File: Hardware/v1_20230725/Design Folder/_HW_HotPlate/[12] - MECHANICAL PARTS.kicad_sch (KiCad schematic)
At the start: 15 parts, among them P1201 MHDR_4X2_RA_2.54MM

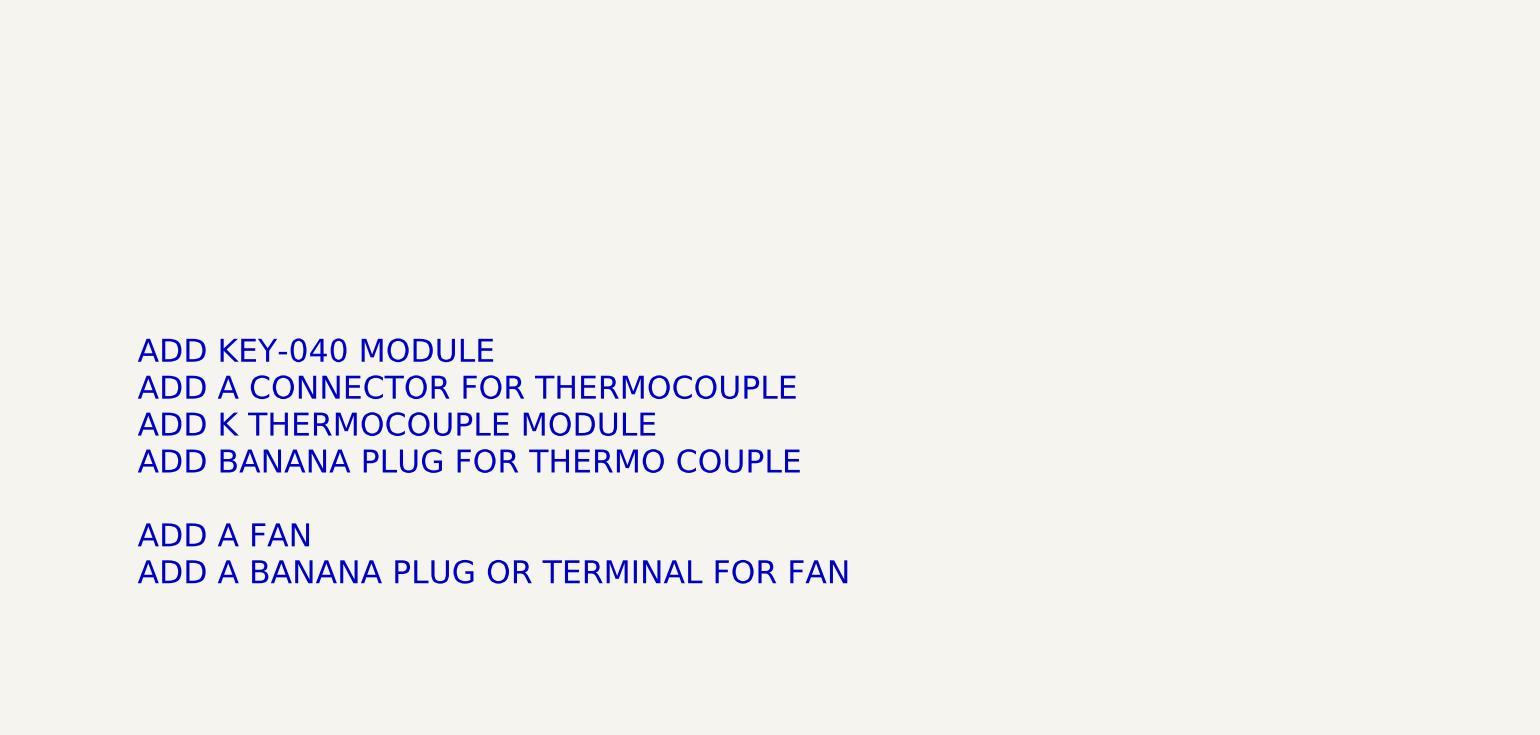
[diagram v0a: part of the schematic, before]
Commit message: Adding some items to todo list
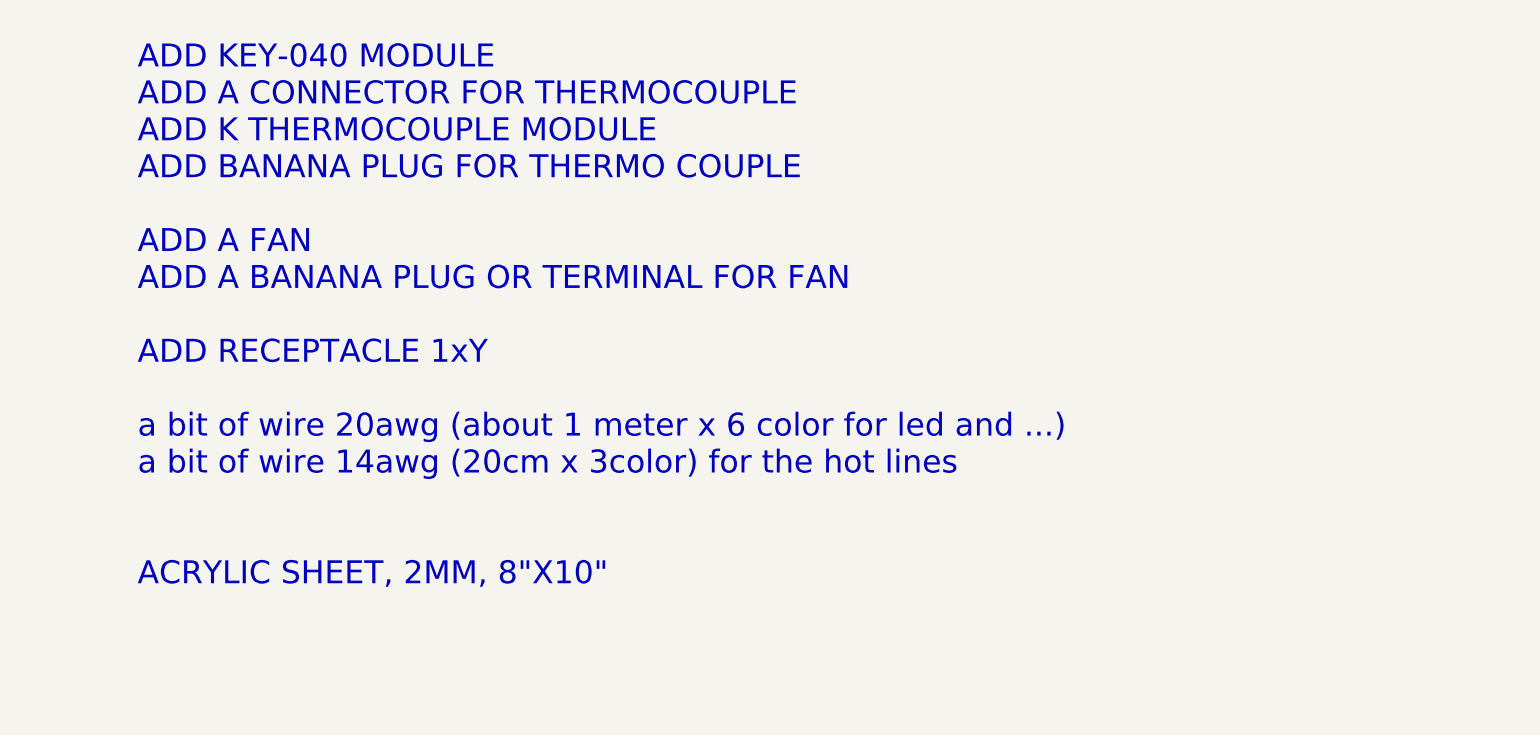
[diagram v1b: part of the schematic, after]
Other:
- note added: "ADD KEY-040 MODULE ADD A CONNECTOR FOR THERMOCOUPLE ADD K THERMOCOUPLE MODULE ADD BANANA PLUG FOR THERMO COUPLE ADD A FAN ADD A BANANA PLUG OR TERMINAL FOR FAN ADD RECEPTACLE 1xY a bit of wire 20awg (about 1 meter x 6 color for led and ...) a bit of wire 14awg (20cm x 3color) for the hot lines ACRYLIC SHEET, 2MM, 8"X10""
- note removed: "ADD KEY-040 MODULE ADD A CONNECTOR FOR THERMOCOUPLE ADD K THERMOCOUPLE MODULE ADD BANANA PLUG FOR THERMO COUPLE ADD A FAN ADD A BANANA PLUG OR TERMINAL FOR FAN"
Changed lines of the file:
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@@
     (effects (font (size 3 3)) (justify left bottom))
   )
-  (text "ADD KEY-040 MODULE\nADD A CONNECTOR FOR THERMOCOUPLE\nADD K THERMOCOUPLE MODULE\nADD BANANA PLUG FOR THERMO COUPLE\n\nADD A FAN \nADD A BANANA PLUG OR TERMINAL FOR FAN"
+  (text "ADD KEY-040 MODULE\nADD A CONNECTOR FOR THERMOCOUPLE\nADD K THERMOCOUPLE MODULE\nADD BANANA PLUG FOR THERMO COUPLE\n\nADD A FAN \nADD A BANANA PLUG OR TERMINAL FOR FAN\n\nADD RECEPTACLE 1xY\n\na bit of wire 20awg (about 1 meter x 6 color for led and ...)\na bit of wire 14awg (20cm x 3color) for the hot lines\n\n\nACRYLIC SHEET, 2MM, 8\"X10\""
     (at 228.6 125.73 0)
     (effects (font (size 3 3)) (justify left bottom))

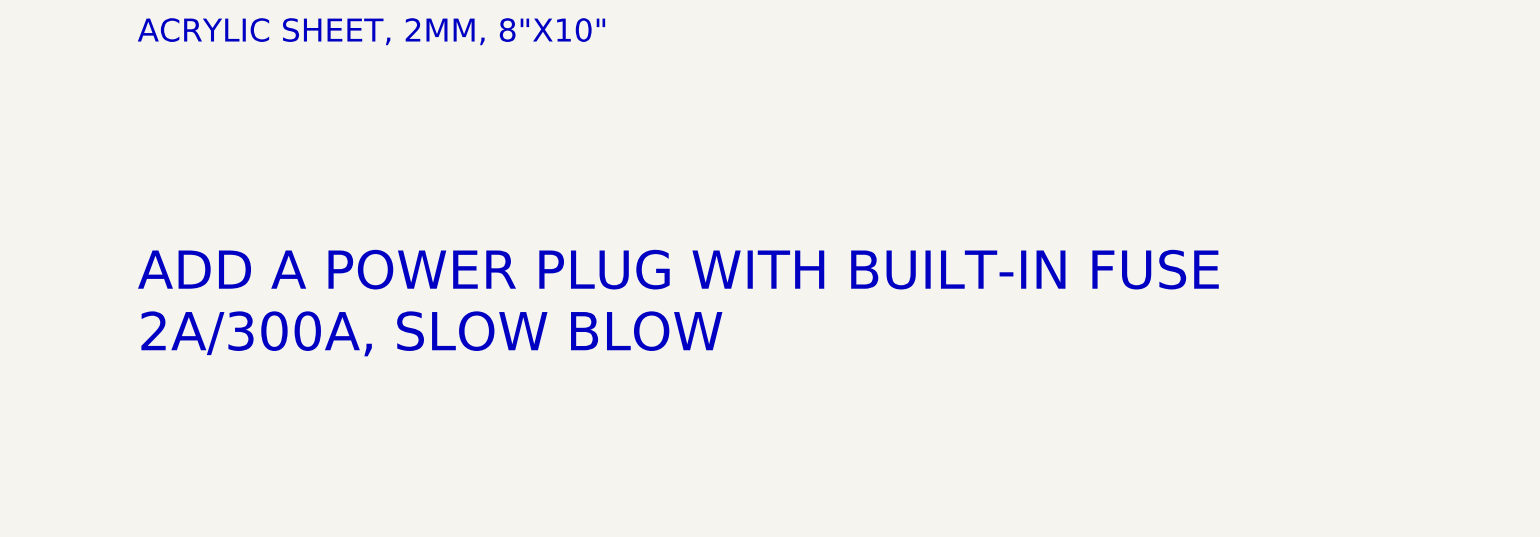
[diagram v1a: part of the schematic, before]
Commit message: A little change in folder structures
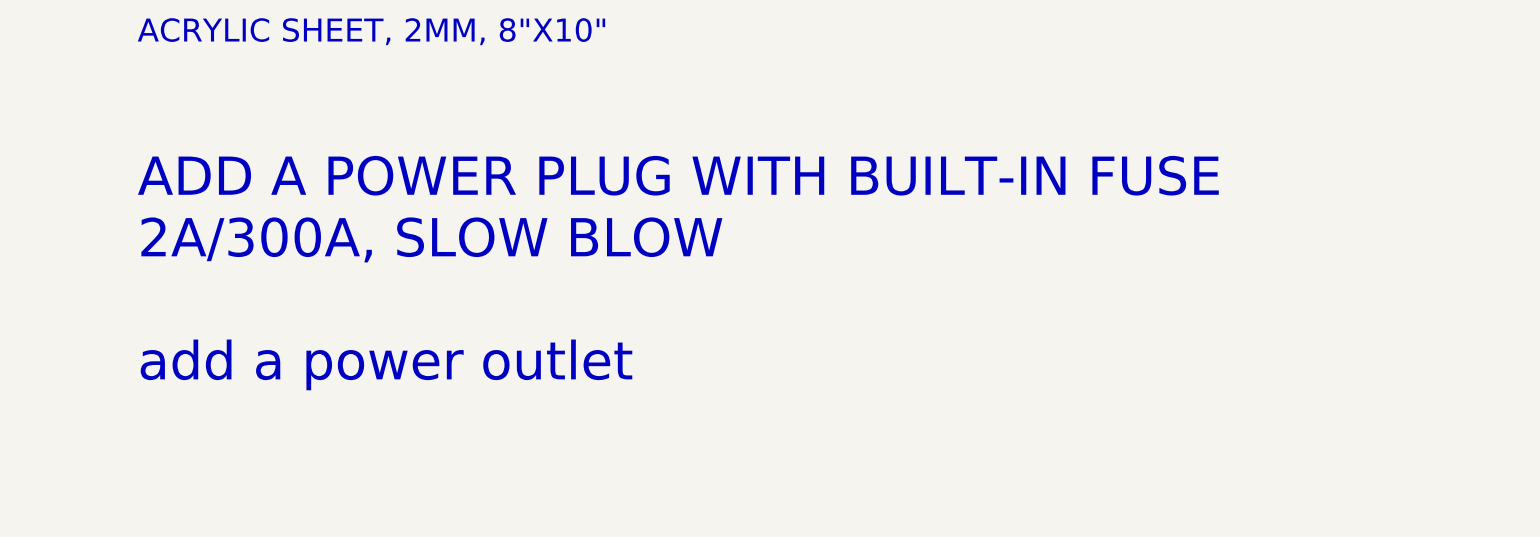
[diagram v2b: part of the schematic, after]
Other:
- note added: "ADD A POWER PLUG WITH BUILT-IN FUSE 2A/300A, SLOW BLOW add a power outlet"
- note removed: "ADD A POWER PLUG WITH BUILT-IN FUSE 2A/300A, SLOW BLOW"
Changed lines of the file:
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@@
     (effects (font (size 3 3)) (justify left bottom))
   )
-  (text "ADD A POWER PLUG WITH BUILT-IN FUSE\n2A/300A, SLOW BLOW"
-    (at 228.6 166.37 0)
+  (text "ADD A POWER PLUG WITH BUILT-IN FUSE\n2A/300A, SLOW BLOW\n\nadd a power outlet"
+    (at 228.6 170.18 0)
     (effects (font (size 5 5)) (justify left bottom))
   )
